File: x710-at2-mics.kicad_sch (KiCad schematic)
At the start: 67 parts, among them U10 74LVC1G07_SOT-753, U9 EZX710AT2_S_LMR5

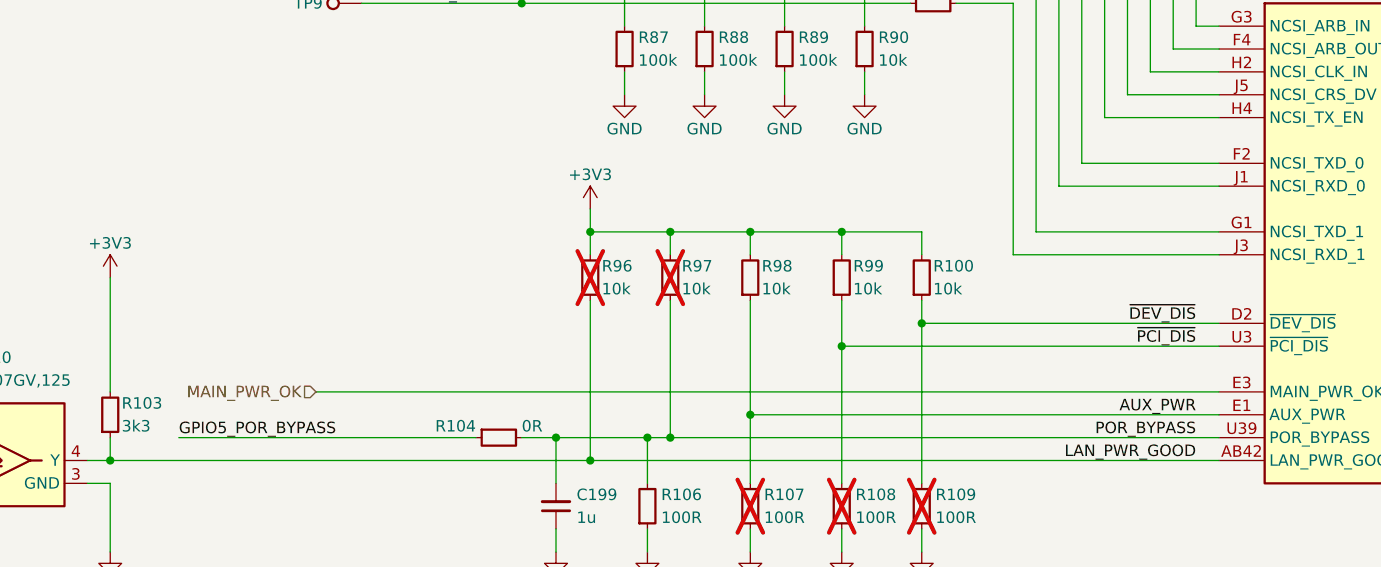
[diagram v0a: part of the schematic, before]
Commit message: [#86617] Add PWR test-points and PGOOD LED, fix MAIN_PWR_OK voltage level
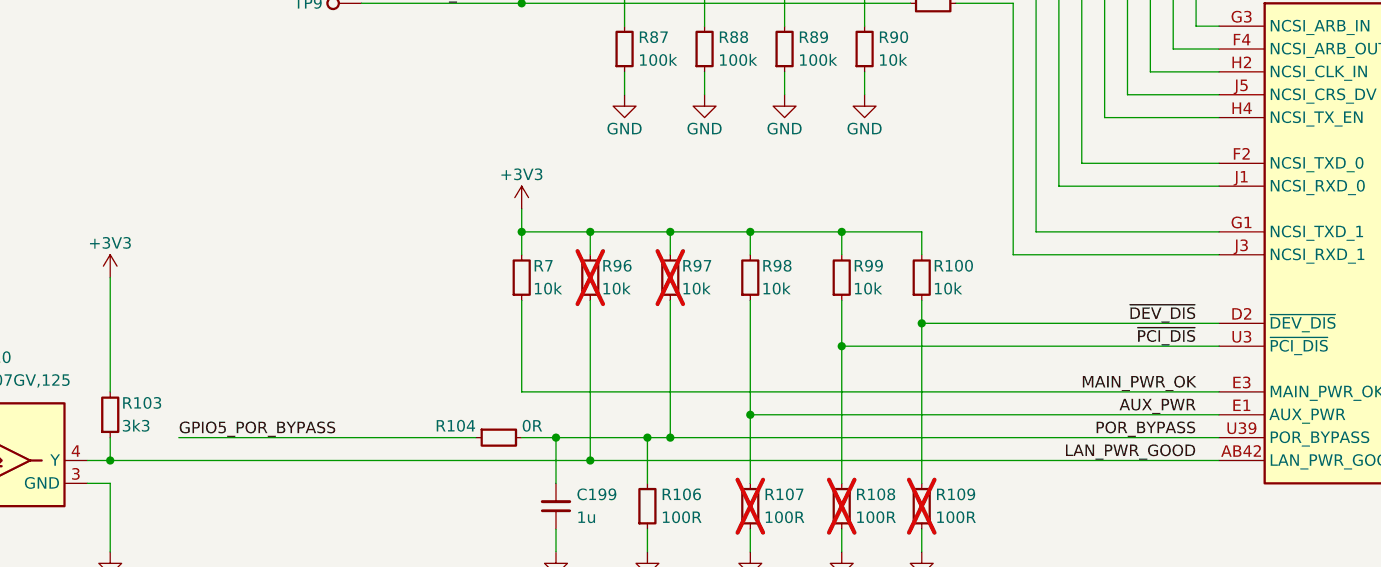
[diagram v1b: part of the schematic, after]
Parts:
- added R7: R_10k_0402, antmicro-footprints:R_0402_1005Metric, symbol antmicroResistors0402:R_10k_0402
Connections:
- net +3V3: now also R7.2
- net MAIN_PWR_OK: now also R7.1
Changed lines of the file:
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@@
 	)
 	(junction
+		(at 110.49 96.52)
+		(diameter 0)
+		(color 0 0 0 0)
+	)
+	(junction
 		(at 127 119.38)
 		(diameter 0)
@@
 	(wire
 		(pts
+			(xy 110.49 96.52) (xy 110.49 99.06)
+		)
+		(stroke
+			(width 0)
+			(type default)
+		)
+	)
+	(wire
+		(pts
 			(xy 135.89 129.54) (xy 135.89 132.08)
 		)
@@
 	(wire
 		(pts
+			(xy 110.49 104.14) (xy 110.49 114.3)
+		)
+		(stroke
+			(width 0)
+			(type default)
+		)
+	)
+	(wire
+		(pts
 			(xy 128.27 66.04) (xy 153.67 66.04)
 		)
@@
 	(wire
 		(pts
-			(xy 118.11 93.98) (xy 118.11 96.52)
+			(xy 110.49 93.98) (xy 110.49 96.52)
 		)
 		(stroke
@@
 	(wire
 		(pts
-			(xy 87.63 114.3) (xy 187.96 114.3)
+			(xy 110.49 114.3) (xy 187.96 114.3)
 		)
 		(stroke
@@
 	(wire
 		(pts
+			(xy 110.49 96.52) (xy 118.11 96.52)
+		)
+		(stroke
+			(width 0)
+			(type default)
+		)
+	)
+	(wire
+		(pts
 			(xy 33.02 106.68) (xy 33.02 104.14)
 		)
@@
 		)
 	)
+	(label "MAIN_PWR_OK"
+		(at 185.42 114.3 180)
+		(effects
+			(font
+				(size 1.27 1.27)
+			)
+			(justify right bottom)
+		)
+	)
 	(label "RSVDP38_VSS"
 		(at 241.3 213.36 0)
@@
 		)
 	)
-	(hierarchical_label "MAIN_PWR_OK"
-		(shape input)
-		(at 87.63 114.3 180)
-		(effects
-			(font
-				(size 1.27 1.27)
-			)
-			(justify right)
-		)
-	)
 	(hierarchical_label "~{PHY_RESET}"
 		(shape input)
@@
 	)
 	(symbol
+		(lib_id "antmicroResistors0402:R_10k_0402")
+		(at 110.49 104.14 90)
+		(unit 1)
+		(exclude_from_sim no)
+		(in_bom yes)
+		(on_board yes)
+		(dnp no)
+		(property "Reference" "R7"
+			(at 111.76 100.33 90)
+			(effects
+				(font
+					(size 1.27 1.27)
+					(thickness 0.15)
+				)
+				(justify right)
+			)
+		)
+		(property "Value" "R_10k_0402"
+			(at 123.19 83.82 0)
+			(effects
+				(font
+					(size 1.27 1.27)
+					(thickness 0.15)
+				)
+				(justify left bottom)
+				(hide yes)
+			)
+		)
+		(property "Footprint" "antmicro-footprints:R_0402_1005Metric"
+			(at 125.73 83.82 0)
+			(effects
+				(font
+					(size 1.27 1.27)
+					(thickness 0.15)
+				)
+				(justify left bottom)
+				(hide yes)
+			)
+		)
+		(property "Datasheet" "https://www.bourns.com/docs/product-datasheets/cr.pdf"
+			(at 128.27 83.82 0)
+			(effects
+				(font
+					(size 1.27 1.27)
+					(thickness 0.15)
+				)
+				(justify left bottom)
+				(hide yes)
+			)
+		)
+		(property "Description" "SMD Chip Resistor, 10 kohm, ± 1%, 62.5 mW, 0402 [1005 Metric], Thick Film, General Purpose"
+			(at 110.49 104.14 0)
+			(effects
+				(font
+					(size 1.27 1.27)
+				)
+				(hide yes)
+			)
+		)
+		(property "MPN" "CR0402-FX-1002GLF"
+			(at 130.81 83.82 0)
+			(effects
+				(font
+					(size 1.27 1.27)
+					(thickness 0.15)
+				)
+				(justify left bottom)
+				(hide yes)
+			)
+		)
+		(property "Manufacturer" "Bourns"
+			(at 133.35 83.82 0)
+			(effects
+				(font
+					(size 1.27 1.27)
+					(thickness 0.15)
+				)
+				(justify left bottom)
+				(hide yes)
+			)
+		)
+		(property "License" "Apache-2.0"
+			(at 135.89 83.82 0)
+			(effects
+				(font
+					(size 1.27 1.27)
+					(thickness 0.15)
+				)
+				(justify left bottom)
+				(hide yes)
+			)
+		)
+		(property "Author" "Antmicro"
+			(at 138.43 83.82 0)
+			(effects
+				(font
+					(size 1.27 1.27)
+					(thickness 0.15)
+				)
+				(justify left bottom)
+				(hide yes)
+			)
+		)
+		(property "Val" "10k"
+			(at 111.76 102.87 90)
+			(effects
+				(font
+					(size 1.27 1.27)
+					(thickness 0.15)
+				)
+				(justify right)
+			)
+		)
+		(property "Tolerance" "1%"
+			(at 120.65 83.82 0)
+			(effects
+				(font
+					(size 1.27 1.27)
+				)
+				(justify left bottom)
+				(hide yes)
+			)
+		)
+		(pin "2"
+		)
+		(pin "1"
+		)
+		(instances
+			(project "10-gbe-expansion"
+				(path "/04bda987-e5eb-48b4-9e90-d8211dc11b39/d0402c84-6d4c-4559-b85a-0c9b588a21c5"
+					(reference "R7")
+					(unit 1)
+				)
+			)
+		)
+	)
+	(symbol
 		(lib_id "antmicroTestPoints:TP_0.75mm_SMD")
 		(at 92.71 55.88 180)
@@
 	(symbol
 		(lib_id "antmicropower:+3V3")
-		(at 118.11 93.98 0)
+		(at 110.49 93.98 0)
 		(unit 1)
 		(exclude_from_sim no)
@@
 		(dnp no)
 		(property "Reference" "#PWR0264"
-			(at 133.35 93.98 0)
+			(at 125.73 93.98 0)
 			(effects
 				(font
@@
 		)
 		(property "Value" "+3V3"
-			(at 118.11 90.17 0)
+			(at 110.49 90.17 0)
 			(effects
 				(font
@@
 		)
 		(property "Footprint" ""
-			(at 133.35 101.6 0)
+			(at 125.73 101.6 0)
 			(effects
 				(font
@@
 		)
 		(property "Datasheet" ""
-			(at 133.35 104.14 0)
+			(at 125.73 104.14 0)
 			(effects
 				(font
@@
 		)
 		(property "Description" ""
-			(at 118.11 93.98 0)
+			(at 110.49 93.98 0)
 			(effects
 				(font
@@
 		)
 		(property "Author" "Antmicro"
-			(at 133.35 96.52 0)
+			(at 125.73 96.52 0)
 			(effects
 				(font
@@
 		)
 		(property "License" "Apache-2.0"
-			(at 133.35 99.06 0)
+			(at 125.73 99.06 0)
 			(effects
 				(font

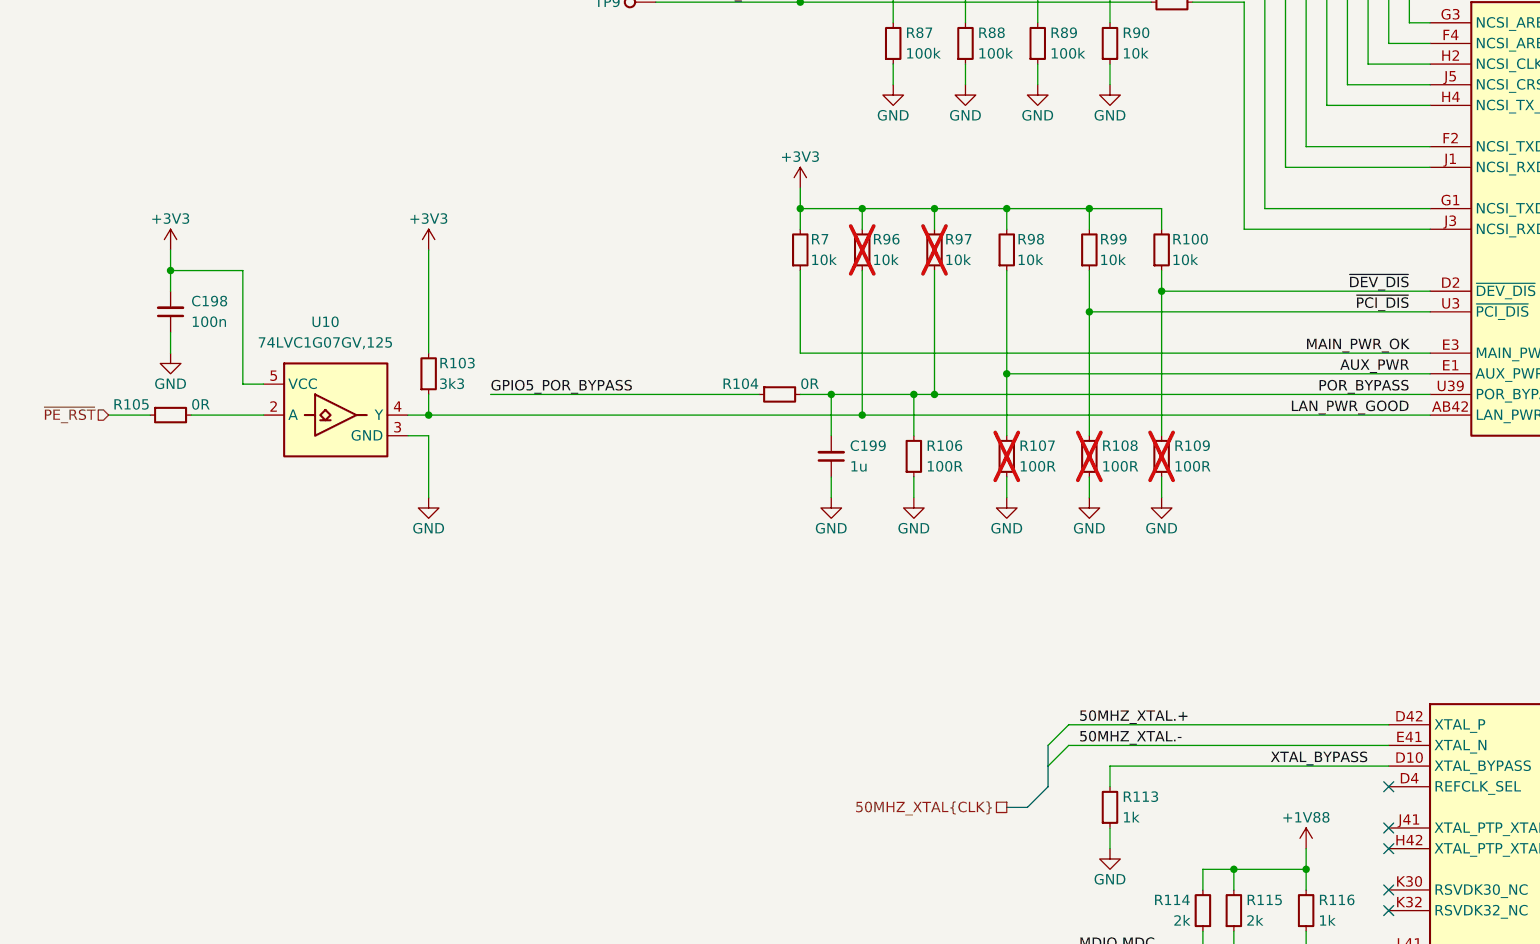
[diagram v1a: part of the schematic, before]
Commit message: [#86617] Power U10 from OCuLink, remove JTAG sheet pin, fix I2C cross
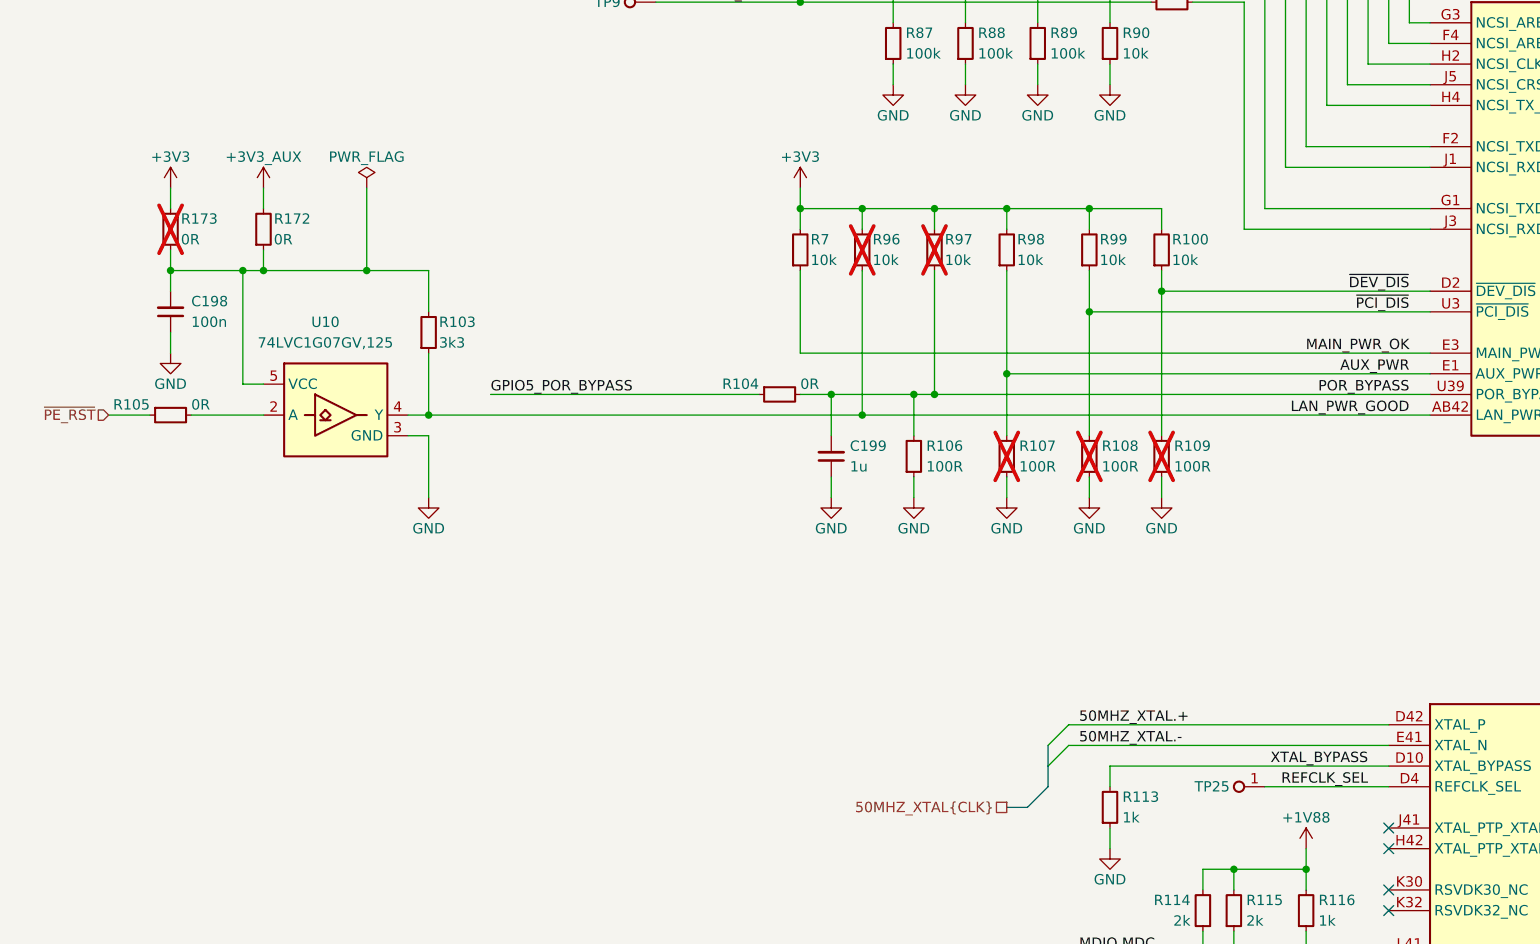
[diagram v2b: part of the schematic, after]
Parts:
- added R172, R173: R_0R_0402, antmicro-footprints:R_0402_1005Metric, symbol antmicroResistors0402:R_0R_0402
- added TP25: TP_0.75mm_SMD, antmicro-footprints:TP_SMD_0.75mm, symbol antmicroTestPoints:TP_0.75mm_SMD
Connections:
- net +3V3: now also R173.2; no longer C198.2, R103.2, U10.5 (VCC)
- net REFCLK_SEL: now reaches U9.D4 (REFCLK_SEL)
- net REFCLK_SEL: now also TP25.1
- new net: C198.2, R103.2, R172.1, R173.1, U10.5 (VCC)
- new net +3V3_AUX: R172.2
- no-connect marks 34 -> 33
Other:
- moved on the sheet: R103

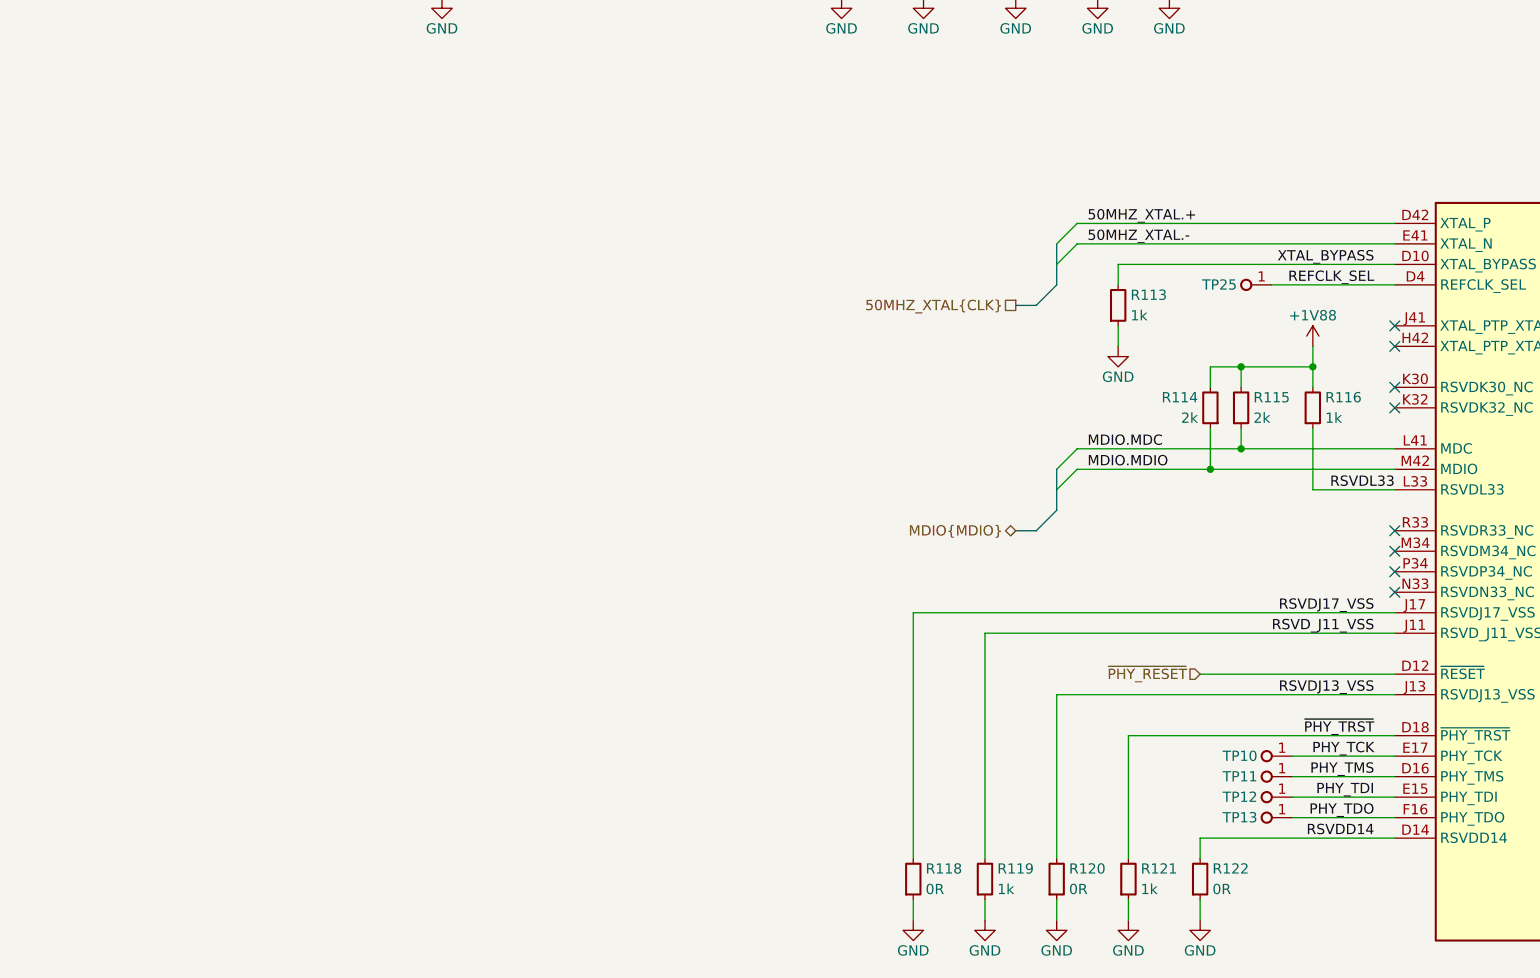
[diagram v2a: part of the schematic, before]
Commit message: [#86617] Remove misc schematic sheet
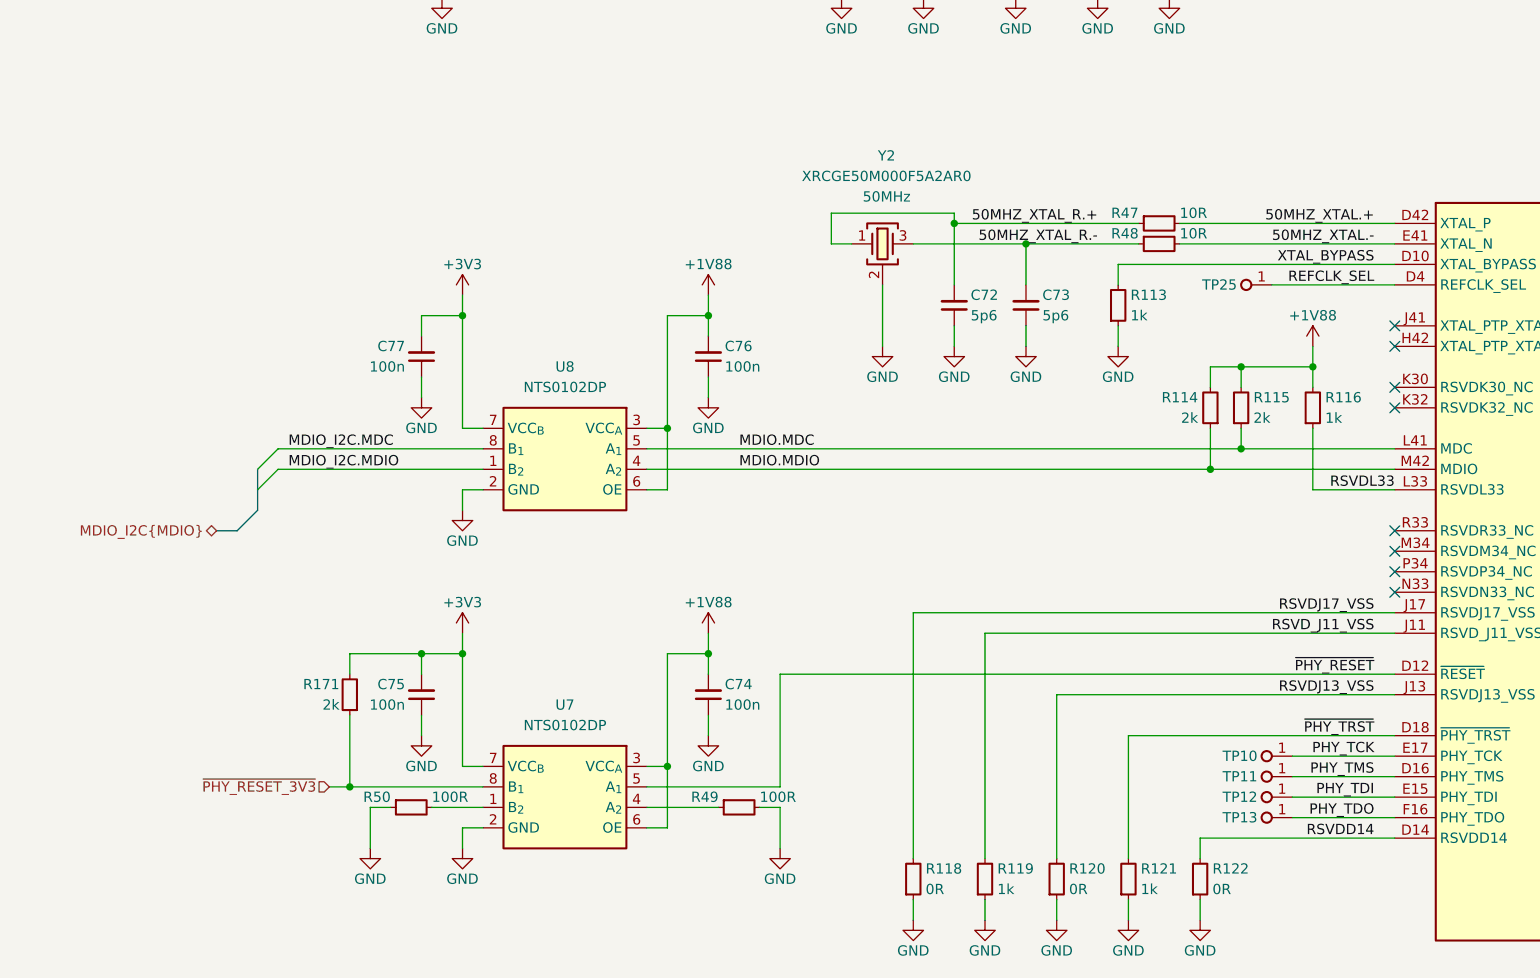
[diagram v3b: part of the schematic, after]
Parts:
- added C72, C73: C_5p6_0402, antmicro-footprints:C_0402_1005Metric, symbol antmicroCapacitors0402:C_5p6_0402
- added C74, C75, C76, C77: C_100n_16V_X7R_0402, antmicro-footprints:C_0402_1005Metric, symbol antmicroCapacitors0402:C_100n_16V_X7R_0402
- added R171: R_2k_0402, antmicro-footprints:R_0402_1005Metric, symbol antmicroResistors0402:R_2k_0402
- added R47, R48: R_10R_0402, antmicro-footprints:R_0402_1005Metric, symbol antmicroResistors0402:R_10R_0402
- added R49, R50: R_100R_0402, antmicro-footprints:R_0402_1005Metric, symbol antmicroResistors0402:R_100R_0402
- added U7, U8: NTS0102_TSSOP, antmicro-footprints:TSSOP-8_3x3mm_P0.65mm, symbol antmicroLogicTranslatorsLevelShifters:NTS0102_TSSOP
- added Y2: Resonator_50MHz_XRCGE, antmicro-footprints:Resonator_SMD_Murata_XRCGB_2x1.6x0.65mm, symbol antmicroResonators:Resonator_50MHz_XRCGE
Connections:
- net +1V88: now also C74.2, C76.2, U7.3 (VCC_{A}), U7.6 (OE), U8.3 (VCC_{A}), U8.6 (OE)
- net +3V3: now also C75.2, C77.2, R171.2, U7.7 (VCC_{B}), U8.7 (VCC_{B})
- net 50MHZ_XTAL.+: now also R47.2
- net 50MHZ_XTAL.-: now also R48.2
- net GND: now also C72.1, C73.1, C74.1, C75.1, C76.1, C77.1, R49.2, R50.1, U7.2 (GND), U8.2 (GND), Y2.2 (SH), Y2.4 (SH)
- net MDIO.MDC: now also U8.5 (A_{1})
- net MDIO.MDIO: now also U8.4 (A_{2})
- net ~{PHY_RESET}: now also U7.5 (A_{1})
- new net: R50.2, U7.1 (B_{2})
- new net: R49.1, U7.4 (A_{2})
- new net 50MHZ_XTAL_R.+: C72.2, R47.1, Y2.1
- new net 50MHZ_XTAL_R.-: C73.2, R48.1, Y2.3
- new net MDIO_I2C.MDC: U8.8 (B_{1})
- new net MDIO_I2C.MDIO: U8.1 (B_{2})
- new net ~{PHY_RESET_3V3}: R171.1, U7.8 (B_{1})

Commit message: [#86351] Rename project
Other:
- title: 10GbE Expansion -> OCuLink to 10GbE adapter
